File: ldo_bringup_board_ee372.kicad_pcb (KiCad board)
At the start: 4 copper layers, 100 x 100 mm, 159 parts, among them J1 VIN, J10 MD_SW_EN, J11 MD_MCU_PU_EN, J12 BUF_EN, J13 VSIG, J14 VSIG_BUF, J15 NR, J16 NOISE_X100, J17 NOISE_X1000, J18 VIN_PROBE, J19 VREF_PROBE, J2 GND, J20 VOUT_PROBE, J21 VG0_PROBE, J22 VG1_PROBE, J23 VG2_PROBE, J24 VG3_PROBE, J25 VG4_PROBE, J3 IBIAS, J4 VOUT, J5 VIN_SMA, J6 VOUT_SMA, J7 GND, J8 5V, J9 MD_MCU_EN, Q1 FDV305N, Q2 FDV305N, Q3 FDV305N, Q4 FDV305N, Q5 FDV305N, Q6 FDV305N, SW1 MD_SW, U1 LDO_DualMode_BGR_EE372, U2 Teensy4.1, U3 INA190A5IDDFR, U4 INA190A5IDDFR, U5 OPA4388IDR, U6 BUF602ID, U7 ADT7310TRZ

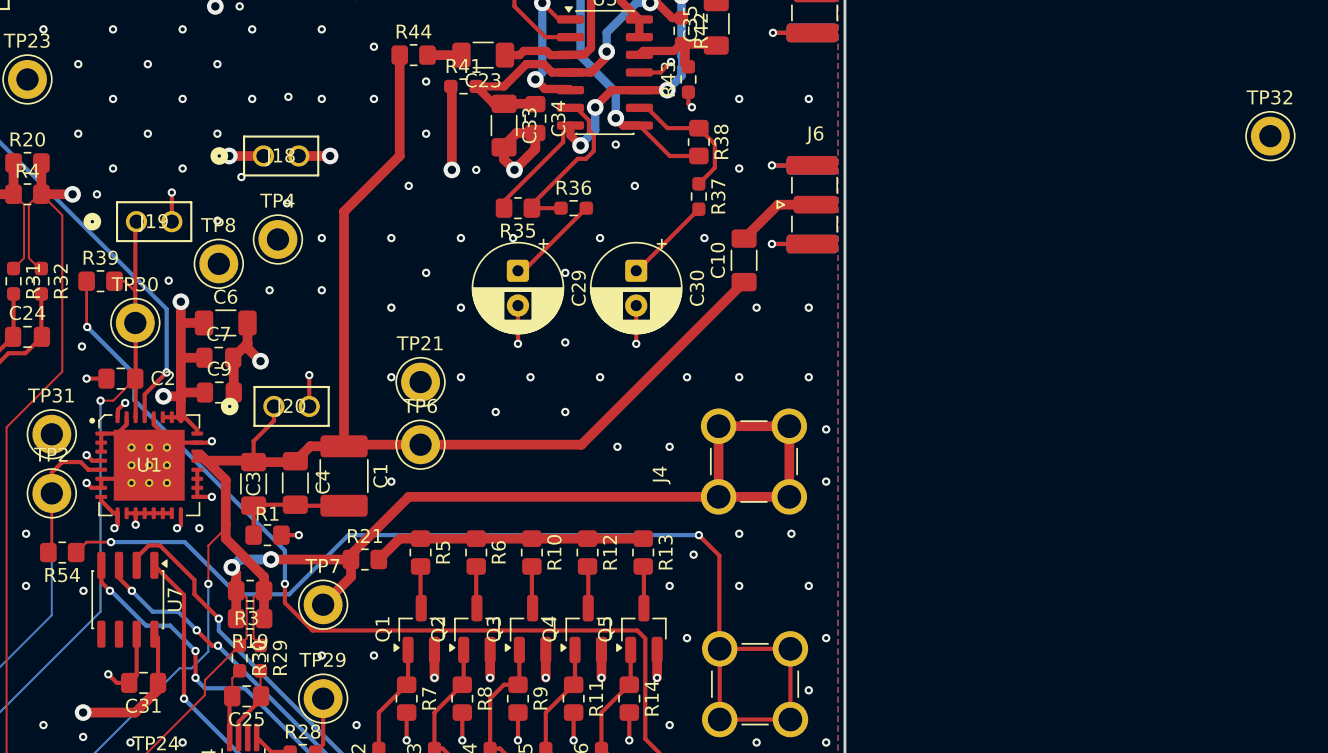
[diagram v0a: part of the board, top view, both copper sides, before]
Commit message: Place TP32, move TP4, TP8 and J19, reroute around them
- TP32 (GND) placed at (165.25, 111.75) by TP7 and TP29, with the J15
  jack track rerouted to make room
- TP8 (GND) moved to (152.25, 85.25), between TP4 and TP30
- TP4 moved to (157.0, 85.25), TP7 nudged, J19 moved 4.75 mm up with its
  NR track
- GND vias around those parts moved or removed

Eleven of the twelve signal test points now have a ground test point
within 5 mm. DRC 0 errors, 0 unconnected, schematic parity 0.
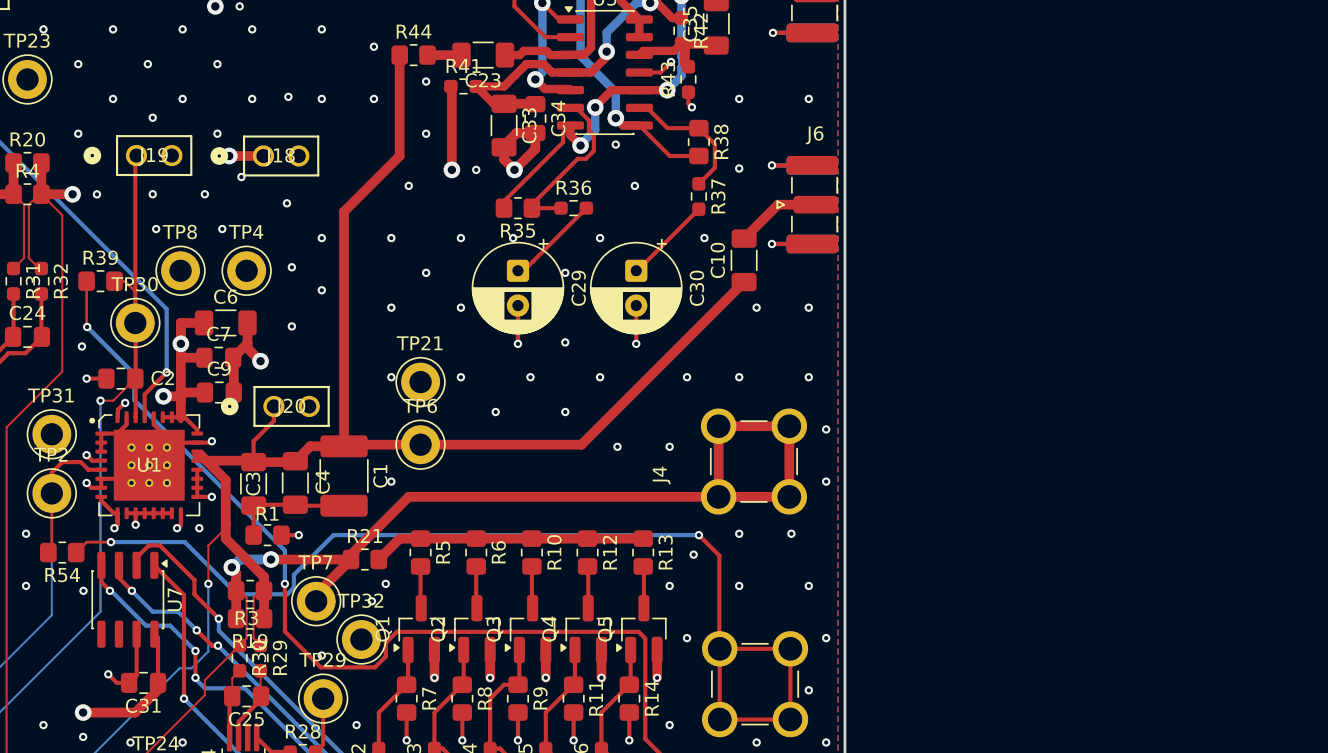
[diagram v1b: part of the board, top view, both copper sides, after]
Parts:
- moved TP32 74.7 mm to (165.2, 111.8)
- moved J19 4.75 mm to (149.1, 77.0)
- moved TP4 3.18 mm to (157.0, 85.2)
- moved TP8 2.80 mm to (152.2, 85.2)
- moved TP7 0.56 mm to (162.0, 109.0)
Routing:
- net GND: track 231.1 -> 224.5 mm, vias 386 -> 385
- net NR: track 55.5 -> 60.2 mm
- net Net-(J15-Pin_1): track 95.6 -> 99.5 mm
- net Net-(J3-Pin_1): track 78.0 -> 78.6 mm
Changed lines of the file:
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@@
 	(footprint "ldo_bringup_board_ee372:CONN_PxC02S_SUL"
 		(layer "F.Cu")
-		(at 149.0849 81.7199)
+		(at 149.0849 76.9699)
 		(tags "PEC02SAAN ")
 		(property "Reference" "J19"
@@
 	(footprint "TestPoint:TestPoint_Keystone_5005-5009_Compact"
 		(layer "F.Cu")
-		(at 159.25 83)
+		(at 157 85.25)
 		(descr "Keystone THM Compact Test Point 5005-5009, http://www.keyelco.com/product-pdf.cfm?p=1314")
 		(tags "Through Hole Mount Test Points")
@@
 	(footprint "TestPoint:TestPoint_Keystone_5005-5009_Compact"
 		(layer "F.Cu")
-		(at 155 84.75)
+		(at 152.25 85.25)
 		(descr "Keystone THM Compact Test Point 5005-5009, http://www.keyelco.com/product-pdf.cfm?p=1314")
 		(tags "Through Hole Mount Test Points")
@@
 	(footprint "TestPoint:TestPoint_Keystone_5005-5009_Compact"
 		(layer "F.Cu")
-		(at 230.575 75.575)
+		(at 165.25 111.75)
 		(descr "Keystone THM Compact Test Point 5005-5009, http://www.keyelco.com/product-pdf.cfm?p=1314")
 		(tags "Through Hole Mount Test Points")
@@
 	(footprint "TestPoint:TestPoint_Keystone_5005-5009_Compact"
 		(layer "F.Cu")
-		(at 162.5 109.25)
+		(at 162 109)
 		(descr "Keystone THM Compact Test Point 5005-5009, http://www.keyelco.com/product-pdf.cfm?p=1314")
 		(tags "Through Hole Mount Test Points")
@@
 	)
 	(segment
-		(start 161.5 95)
-		(end 161.5 92.75)
-		(width 0.3)
-		(layer "F.Cu")
-		(net "GND")
-	)
-	(segment
 		(start 110.5 89)
 		(end 110.5 91.75)
@@
 	)
 	(segment
-		(start 160.75 77)
-		(end 163 77)
-		(width 0.7)
-		(layer "F.Cu")
-		(net "GND")
-	)
-	(segment
 		(start 133.75 86.075)
 		(end 133.675 86)
@@
 	)
 	(segment
-		(start 151.6249 79.6251)
-		(end 151.6249 81.7199)
-		(width 0.3)
-		(layer "F.Cu")
-		(net "GND")
-	)
-	(segment
 		(start 186.5 112.5)
 		(end 186.5 114.5)
@@
 	)
 	(via
+		(at 167 107.75)
+		(size 0.6)
+		(drill 0.3)
+		(layers "F.Cu" "B.Cu")
+		(net "GND")
+	)
+	(via
 		(at 189.9 140.4)
 		(size 0.6)
@@
 	)
 	(via
-		(at 161.5 92.75)
-		(size 0.6)
-		(drill 0.3)
-		(layers "F.Cu" "B.Cu")
-		(net "GND")
-	)
-	(via
 		(at 192.4 137.9)
 		(size 0.6)
@@
 	)
 	(via
-		(at 163 77)
-		(size 1.2)
-		(drill 0.6)
-		(layers "F.Cu" "B.Cu")
-		(net "GND")
-	)
-	(via
 		(at 159.9 65.4)
 		(size 0.6)
@@
 	)
 	(via
-		(at 149.9 75.4)
+		(at 150.25 79.75)
 		(size 0.6)
 		(drill 0.3)
@@
 	)
 	(via
-		(at 166.15 112.9)
+		(at 166 109)
 		(size 0.6)
 		(drill 0.3)
@@
 	)
 	(via
+		(at 155.25 82.25)
+		(size 0.6)
+		(drill 0.3)
+		(layers "F.Cu" "B.Cu")
+		(net "GND")
+	)
+	(via
 		(at 167.4 57.9)
 		(size 0.6)
@@
 	)
 	(via
-		(at 147.4 77.9)
+		(at 150.25 74.25)
 		(size 0.6)
 		(drill 0.3)
@@
 	)
 	(via
-		(at 152.4 77.9)
+		(at 154 79.75)
 		(size 0.6)
 		(drill 0.3)
@@
 	)
 	(via
-		(at 154.9 81.65)
+		(at 160.25 85)
 		(size 0.6)
 		(drill 0.3)
@@
 	)
 	(via
-		(at 151.6249 79.6251)
-		(size 0.6)
-		(drill 0.3)
-		(layers "F.Cu" "B.Cu")
-		(net "GND")
-	)
-	(via
 		(at 119.9 65.4)
 		(size 0.6)
@@
 	)
 	(via
-		(at 158.65 86.65)
+		(at 160.25 89.25)
 		(size 0.6)
 		(drill 0.3)
@@
 	)
 	(via
-		(at 151.4 85.959455)
+		(at 150.5 82.25)
 		(size 0.6)
 		(drill 0.3)
@@
 	)
 	(segment
+		(start 164.5 106)
+		(end 162 108.5)
+		(width 0.7)
+		(layer "F.Cu")
+		(net "SHUNT_OUT_B")
+	)
+	(segment
 		(start 156.25 108.25)
 		(end 156.5 108.25)
@@
 	)
 	(segment
-		(start 164.5 107.25)
-		(end 162.5 109.25)
-		(width 0.7)
-		(layer "F.Cu")
-		(net "SHUNT_OUT_B")
-	)
-	(segment
 		(start 156.25 110.25)
 		(end 156.25 110.5)
@@
 	)
 	(segment
-		(start 164.5 106)
-		(end 164.5 107.25)
+		(start 162 108.5)
+		(end 162 109)
 		(width 0.7)
 		(layer "F.Cu")
@@
 	)
 	(segment
-		(start 190.46 123.71)
-		(end 190.46 128.96)
+		(start 162.330761 113.75)
+		(end 166.219239 113.75)
 		(width 0.3)
 		(layer "F.Cu")
@@
 	)
 	(segment
-		(start 159.75 107.75)
-		(end 159.75 109.116296)
+		(start 167 112)
+		(end 167.8 111.2)
 		(width 0.3)
 		(layer "F.Cu")
@@
 	)
 	(segment
+		(start 159.75 111.169239)
+		(end 162.330761 113.75)
+		(width 0.3)
+		(layer "F.Cu")
+		(net "Net-(J15-Pin_1)")
+	)
+	(segment
+		(start 167.8 111.2)
+		(end 185.17478 111.2)
+		(width 0.3)
+		(layer "F.Cu")
+		(net "Net-(J15-Pin_1)")
+	)
+	(segment
+		(start 185.65 118.9)
+		(end 190.46 123.71)
+		(width 0.3)
+		(layer "F.Cu")
+		(net "Net-(J15-Pin_1)")
+	)
+	(segment
 		(start 195.54 134.04)
 		(end 195.54 128.96)
@@
 	)
 	(segment
-		(start 185.07478 111.1)
-		(end 185.65 111.67522)
+		(start 159.75 107.75)
+		(end 159.75 111.169239)
 		(width 0.3)
 		(layer "F.Cu")
@@
 	)
 	(segment
-		(start 185.65 118.9)
-		(end 190.46 123.71)
+		(start 166.219239 113.75)
+		(end 167 112.969239)
 		(width 0.3)
 		(layer "F.Cu")
@@
 	)
 	(segment
-		(start 159.75 109.116296)
-		(end 161.733704 111.1)
+		(start 167 112.969239)
+		(end 167 112)
 		(width 0.3)
 		(layer "F.Cu")
@@
 	)
 	(segment
-		(start 161.733704 111.1)
-		(end 185.07478 111.1)
+		(start 190.46 123.71)
+		(end 190.46 128.96)
+		(width 0.3)
+		(layer "F.Cu")
+		(net "Net-(J15-Pin_1)")
+	)
+	(segment
+		(start 185.17478 111.2)
+		(end 185.65 111.67522)
 		(width 0.3)
 		(layer "F.Cu")
@@
 	)
 	(segment
-		(start 149 86.75)
-		(end 149 81.8048)
-		(width 0.3)
-		(layer "F.Cu")
-		(net "NR")
-	)
-	(segment
 		(start 138.75 117.5)
 		(end 134.51 121.74)
@@
 	)
 	(segment
-		(start 149 81.8048)
-		(end 149.0849 81.7199)
+		(start 149 77.0548)
+		(end 149.0849 76.9699)
 		(width 0.3)
 		(layer "F.Cu")
@@
 		(net "NR")
 	)
+	(segment
+		(start 149 86.75)
+		(end 149 77.0548)
+		(width 0.3)
+		(layer "F.Cu")
+		(net "NR")
+	)
 	(via
 		(at 146.5 94.584898)
@@
 	)
 	(segment
-		(start 152.275 87.475)
-		(end 152.275 89)
-		(width 0.7)
-		(layer "F.Cu")
-		(net "SHUNT_IN_B")
-	)
-	(segment
 		(start 153.45 96.675)
 		(end 153.45 96.95)
@@
 	)
 	(segment
+		(start 152.275 90.5)
+		(end 152.275 89)
+		(width 0.7)
+		(layer "F.Cu")
+		(net "SHUNT_IN_B")
+	)
+	(segment
 		(start 145.9 98.9)
 		(end 146.55 98.9)
@@
 	)
 	(via
-		(at 152.275 87.475)
+		(at 152.275 90.5)
 		(size 1.2)
 		(drill 0.6)
@@
 	)
 	(segment
-		(start 160.060661 108.5)
-		(end 156.310661 108.5)
+		(start 163.25 104.25)
+		(end 160.4 107.1)
 		(width 0.3)
 		(layer "B.Cu")
@@
 	)
 	(segment
-		(start 189.5 104.25)
-		(end 164.310661 104.25)
+		(start 156.310661 108.5)
+		(end 152.560661 104.75)
 		(width 0.3)
 		(layer "B.Cu")
@@
 	)
 	(segment
-		(start 156.310661 108.5)
-		(end 152.560661 104.75)
+		(start 160.4 108.019239)
+		(end 159.919239 108.5)
+		(width 0.3)
+		(layer "B.Cu")
+		(net "Net-(J3-Pin_1)")
+	)
+	(segment
+		(start 159.919239 108.5)
+		(end 156.310661 108.5)
+		(width 0.3)
+		(layer "B.Cu")
+		(net "Net-(J3-Pin_1)")
+	)
+	(segment
+		(start 189.5 104.25)
+		(end 163.25 104.25)
 		(width 0.3)
 		(layer "B.Cu")
@@
 	)
 	(segment
-		(start 164.310661 104.25)
-		(end 160.060661 108.5)
+		(start 160.4 107.1)
+		(end 160.4 108.019239)
 		(width 0.3)
 		(layer "B.Cu")

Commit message: Add three spare through-hole pads, TP35 to TP37
Keystone test point footprints valued SP1, SP2 and SP3, marked DNP and
left unconnected, placed along the top edge at y = 55.5. GND stitching
vias near them moved, four added and one removed.

161 parts, 112 nets. DRC 0 errors, 0 unconnected, schematic parity 0.
ERC 0 errors.
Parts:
- added TP35: SP1, TestPoint:TestPoint_Keystone_5005-5009_Compact, F.Cu at (165.8, 55.5)
- added TP36: SP2, TestPoint:TestPoint_Keystone_5005-5009_Compact, F.Cu at (171.2, 55.5)
- added TP37: SP3, TestPoint:TestPoint_Keystone_5005-5009_Compact, F.Cu at (176.5, 55.5)
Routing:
- net GND: vias 385 -> 388
